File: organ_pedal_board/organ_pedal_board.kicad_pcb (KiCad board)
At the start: 2 copper layers, 100 x 100 mm, 38 parts, among them J1 Conn_01x04, J2 NMJ6HFD2, J3 NMJ6HFD2, J4 ADS1115_conn, SW1 SW_Push, SW2 SW_Push, SW3 SW_Push, SW4 SW_Push, SW5 SW_Push, SW6 SW_Push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

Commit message: Update active layer and pad dimensions in organ pedal board design
- Changed active layer from 25 to 5 in the project settings.
- Updated pad drill size from 0.8 to 2.0, height from 1.27 to 4.0, and width from 2.54 to 4.0 for improved component compatibility.
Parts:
- added G***: LOGO, LOGO, F.Cu at (174.5, 71.0)
- added G***: LOGO, LOGO, F.Cu at (174.0, 111.0)
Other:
- outline, holes or cut-outs redrawn
- board text added: "Ad majorem Dei gloriam!"
- board text added: "Juntos pela música sacra"

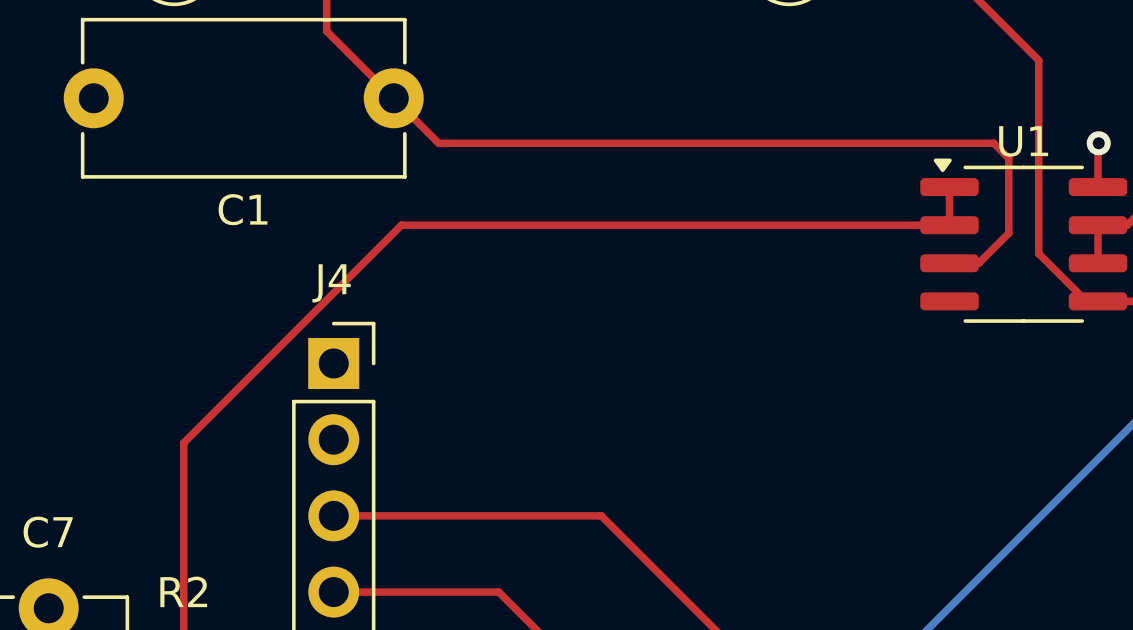
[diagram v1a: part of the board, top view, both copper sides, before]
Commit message: Fix: Corrected MCP6002 power supply, corrected P10 plug 1 MCP6002  signal output
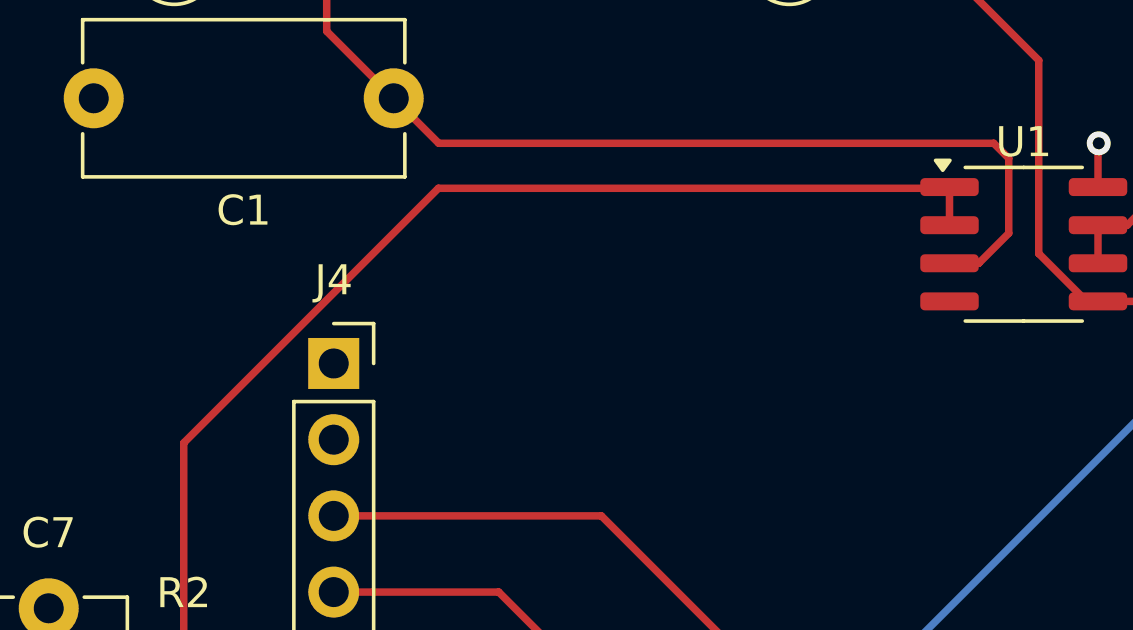
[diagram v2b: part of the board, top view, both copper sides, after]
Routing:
- net Net-(U1A--): track 38.0 -> 38.5 mm
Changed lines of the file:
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@@
+			(polygon
+				(pts
+					(xy 209.958245 94.060415) (xy 210.081344 94.060415) (xy 210.847289 94.818453) (xy 210.717352 94.973822)
+					(xy 209.958245 94.478864)
+				)
+			)
 			(polygon
 				(pts
@@
 	)
 	(segment
-		(start 132.375 106.988)
-		(end 139.633 99.73)
+		(start 157.86 98.5)
+		(end 157.9 98.46)
+		(width 0.25)
+		(layer "F.Cu")
+		(net 17)
+	)
+	(segment
+		(start 132.375 115.185)
+		(end 132.375 106.988)
+		(width 0.25)
+		(layer "F.Cu")
+		(net 17)
+	)
+	(segment
+		(start 140.863 98.5)
+		(end 157.86 98.5)
 		(width 0.25)
 		(layer "F.Cu")
@@
 	)
 	(segment
-		(start 139.633 99.73)
-		(end 157.9 99.73)
-		(width 0.25)
-		(layer "F.Cu")
-		(net 17)
-	)
-	(segment
-		(start 132.375 115.185)
-		(end 132.375 106.988)
-		(width 0.25)
-		(layer "F.Cu")
+		(start 132.375 106.988)
+		(end 140.863 98.5)
+		(width 0.25)
+		(layer "F.Cu")

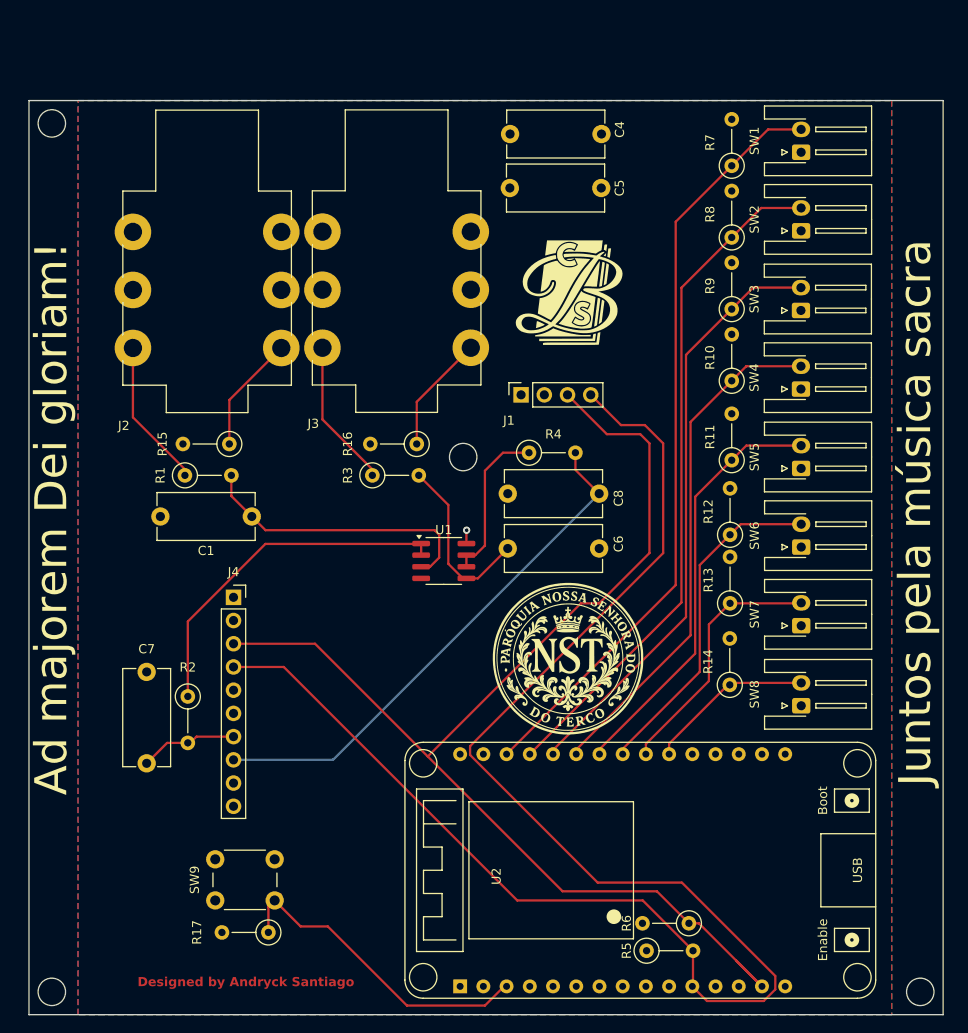
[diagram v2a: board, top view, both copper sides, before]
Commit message: Fix: Corrected vias and esp32 pin assignment
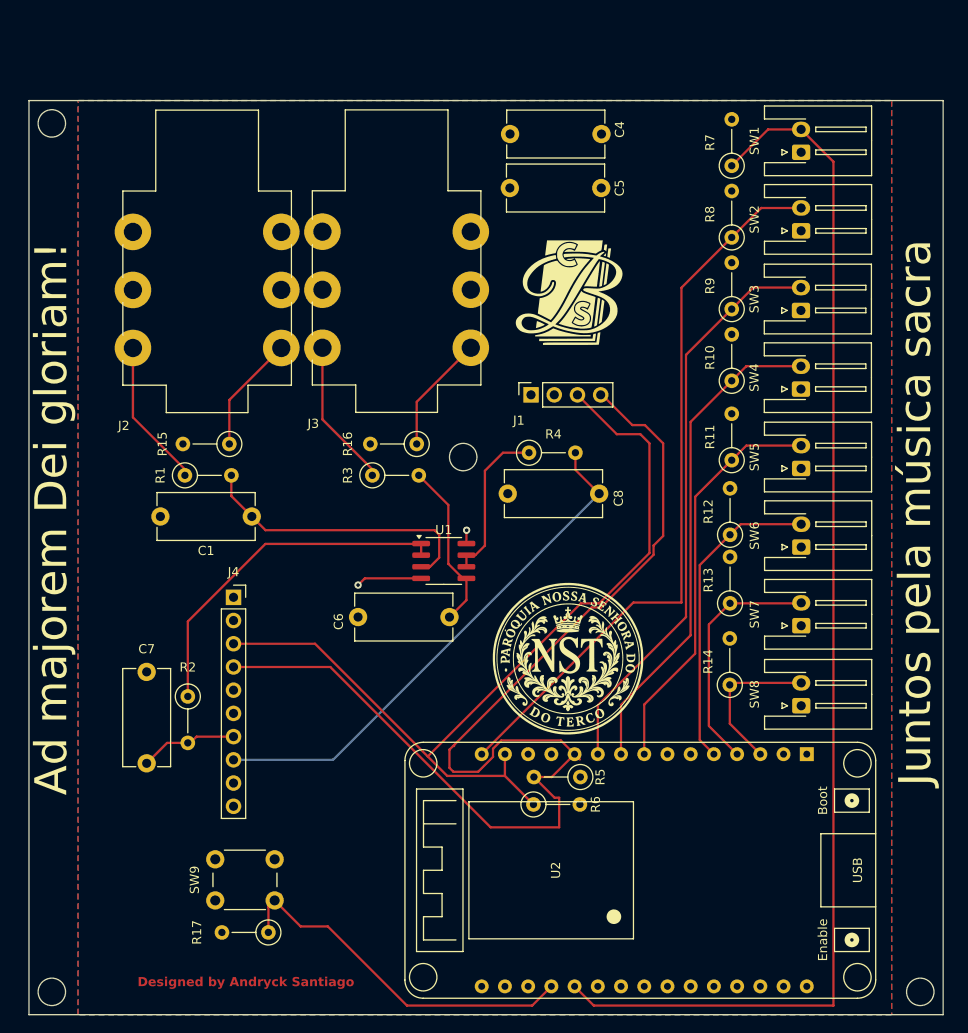
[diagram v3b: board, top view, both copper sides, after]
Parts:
- moved R6 21.4 mm to (170.2, 127.0), turned to 0 degrees
- moved R5 20.3 mm to (175.3, 124.0), turned to 180 degrees
- moved C6 9.84 mm to (161.0, 106.5), turned to 180 degrees
- moved J1 1.09 mm to (169.9, 82.2)
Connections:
- C1 pad 2: GND -> +3.3V
- U1 pad 4: +3.3V -> GND
- U1 pad 8: GND -> +3.3V
- U2 pad 10: unconnected-(U2-D19-Pad10) -> /button3
- U2 pad 15: unconnected-(U2-D23-Pad15) -> /button2
- U2 pad 19: unconnected-(U2-D34-Pad19) -> /config_button
- U2 pad 20: unconnected-(U2-D35-Pad20) -> /button1
- U2 pad 21: /button8 -> unconnected-(U2-D32-Pad21)
- U2 pad 22: /button7 -> unconnected-(U2-D33-Pad22)
- U2 pad 23: /button6 -> unconnected-(U2-D25-Pad23)
- U2 pad 24: /button5 -> unconnected-(U2-D26-Pad24)
- U2 pad 25: /button4 -> unconnected-(U2-D27-Pad25)
- U2 pad 26: /button3 -> unconnected-(U2-D14-Pad26)
- U2 pad 27: /button2 -> unconnected-(U2-D12-Pad27)
- U2 pad 28: /button1 -> unconnected-(U2-D13-Pad28)
- U2 pad 3: /config_button -> /button8
- U2 pad 4: unconnected-(U2-D2-Pad4) -> /button7
- U2 pad 5: unconnected-(U2-D4-Pad5) -> /button6
- U2 pad 8: unconnected-(U2-D5-Pad8) -> /button5
- U2 pad 9: unconnected-(U2-D18-Pad9) -> /button4
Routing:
- net /button1: track 83.8 -> 135.7 mm
- net /i2c_sda: track 175.1 -> 127.8 mm
- net /i2c_scl: track 133.9 -> 98.0 mm
- net GND: track 1.47 -> 7.20 mm
- net /config_button: track 35.7 -> 40.6 mm
- net /button2: track 75.0 -> 79.9 mm
- net /button6: track 37.1 -> 34.3 mm
- net /button5: track 46.4 -> 44.4 mm
- net /button7: track 28.1 -> 26.5 mm
- net /button3: track 65.3 -> 63.8 mm
- net /button4: track 56.1 -> 54.7 mm
- net /button8: track 18.4 -> 17.1 mm
- net Net-(U1B-+): track 19.5 -> 18.6 mm
- net +3.3V: track 0.64 -> 1.47 mm, vias 0 -> 1

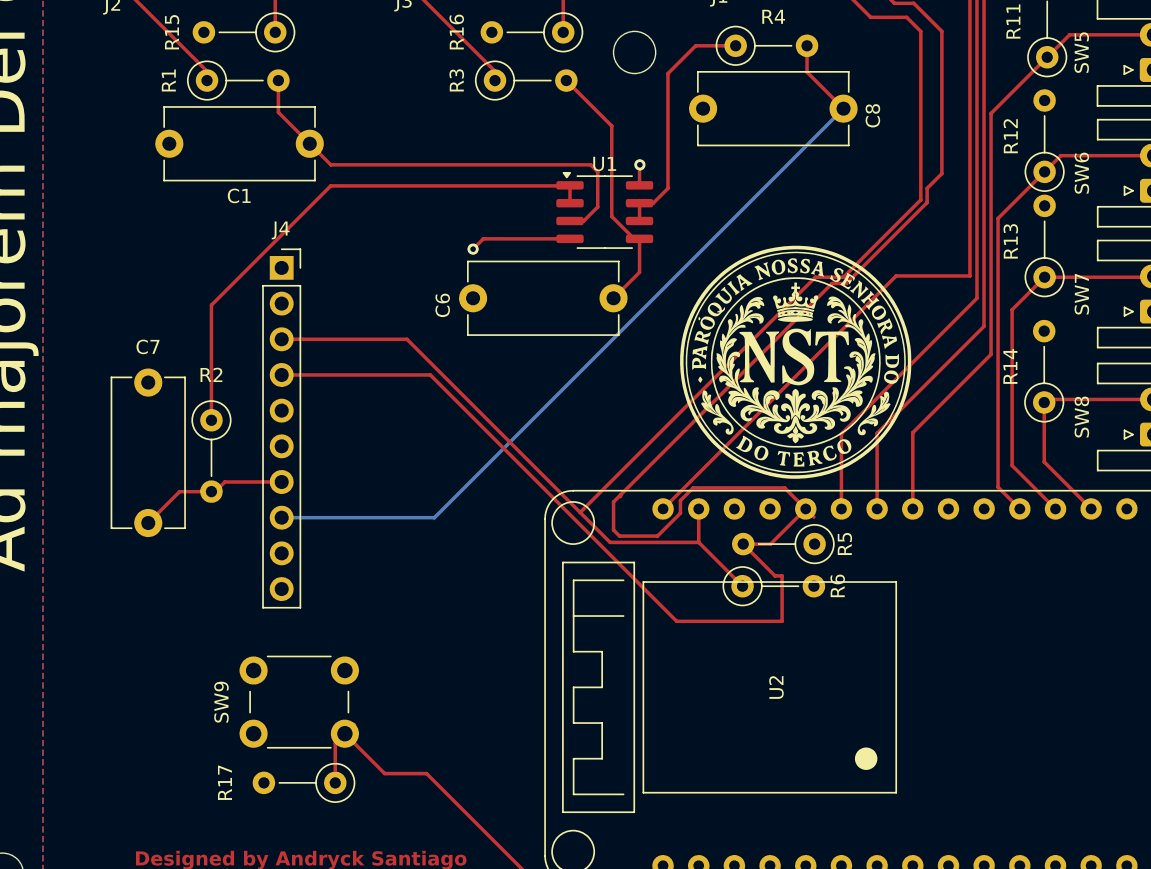
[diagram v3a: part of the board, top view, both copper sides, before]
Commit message: Fix: Component placement enhancement
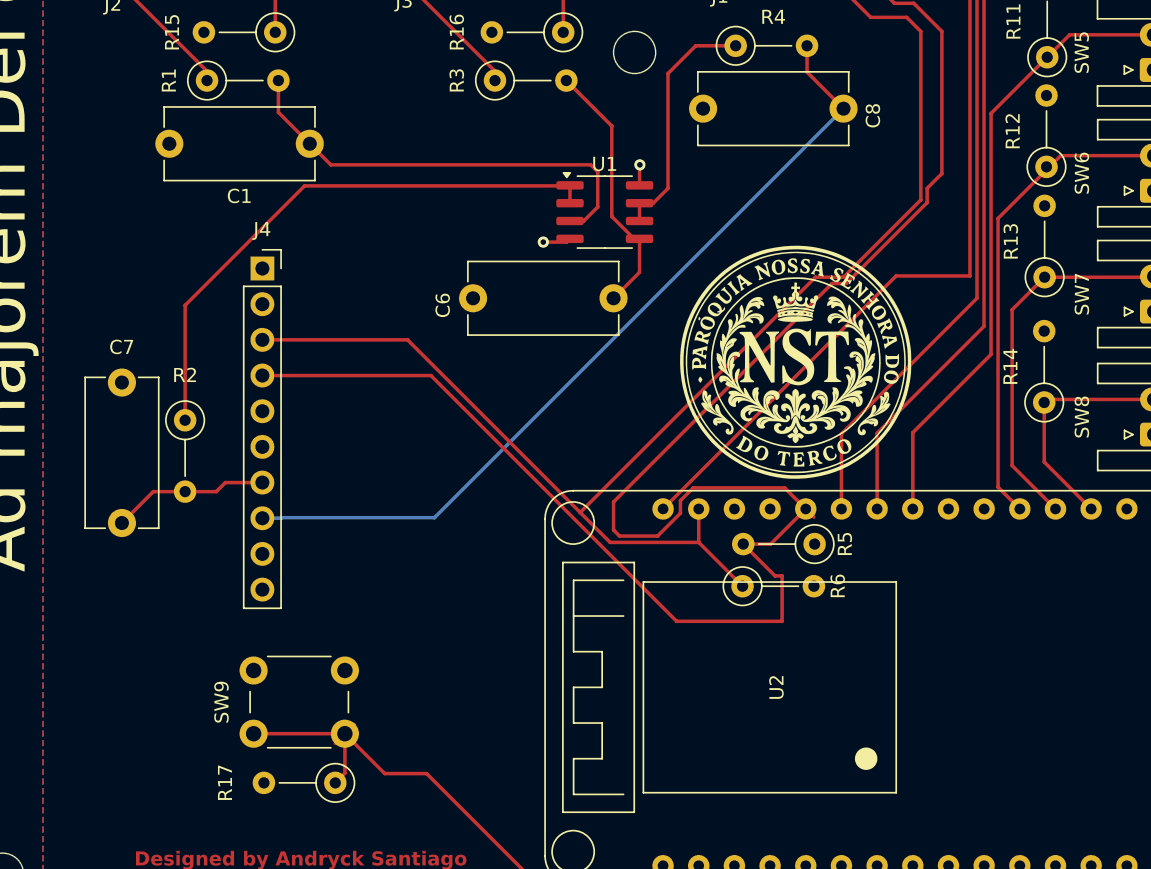
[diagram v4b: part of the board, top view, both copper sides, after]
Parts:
- moved C7 1.88 mm to (126.0, 122.5)
- moved R2 1.88 mm to (130.5, 115.2)
- moved J4 1.38 mm to (136.0, 104.4)
- moved R12 0.38 mm to (191.8, 97.1)
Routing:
- net /config_button: track 40.6 -> 48.1 mm
- net GND: track 7.20 -> 2.00 mm
- net Net-(U1A--): track 38.5 -> 40.4 mm
- net /pedal2_signal: track 57.6 -> 59.0 mm
- net /i2c_scl: track 98.0 -> 99.4 mm
- net /i2c_sda: track 127.8 -> 129.1 mm
